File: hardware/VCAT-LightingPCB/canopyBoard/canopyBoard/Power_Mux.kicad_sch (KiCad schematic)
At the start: 6 parts, among them U15 TPS2117DRLR

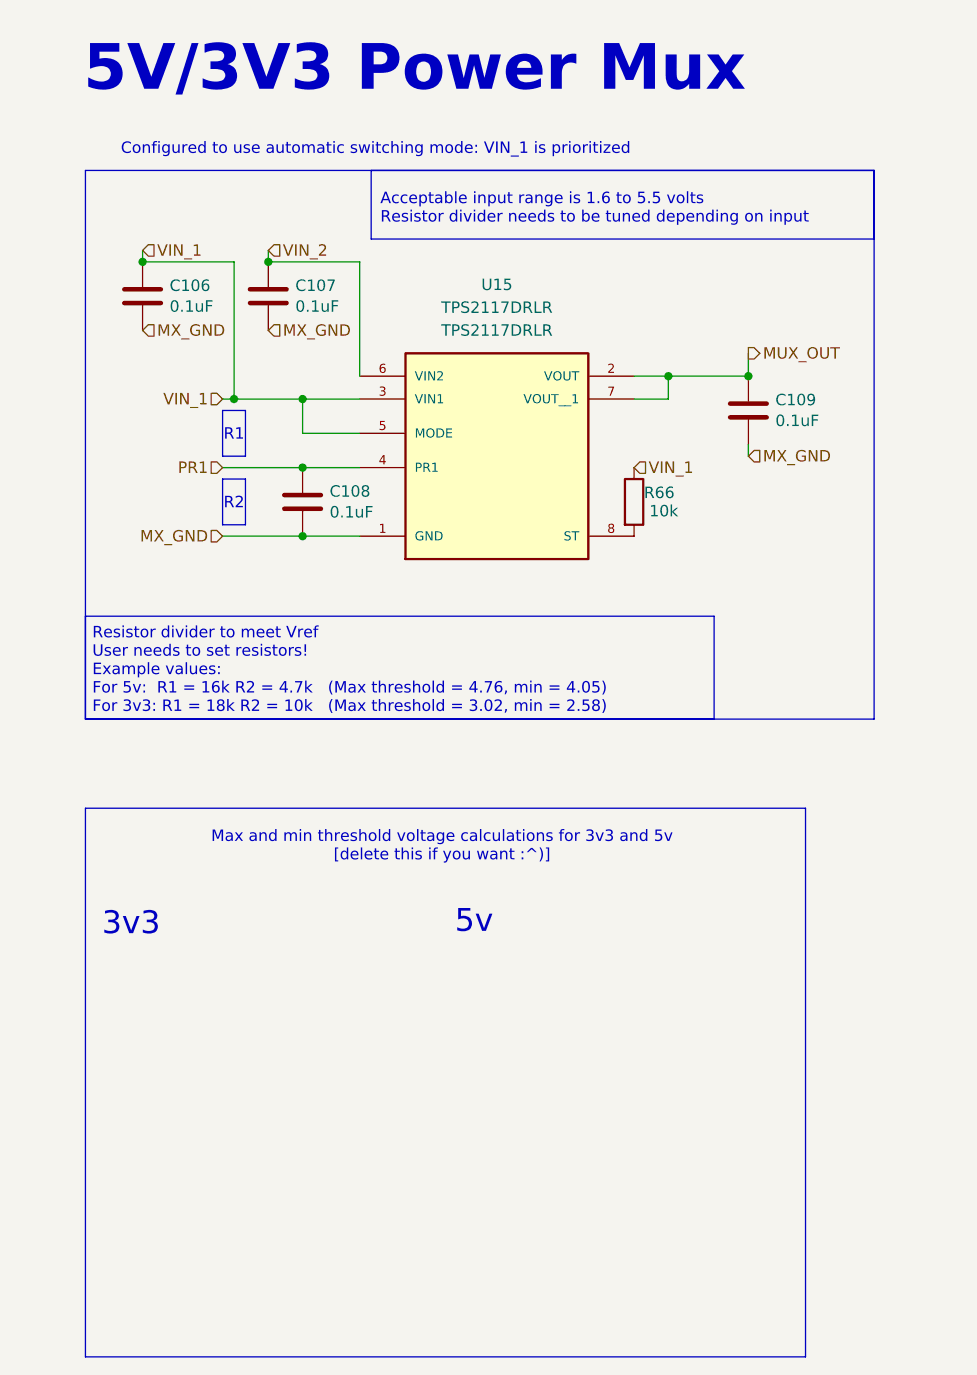
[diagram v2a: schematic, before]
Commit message: Untrack KiCad .history, convert KiCAD-Sharepoint to a submodule, remove LightsPCB
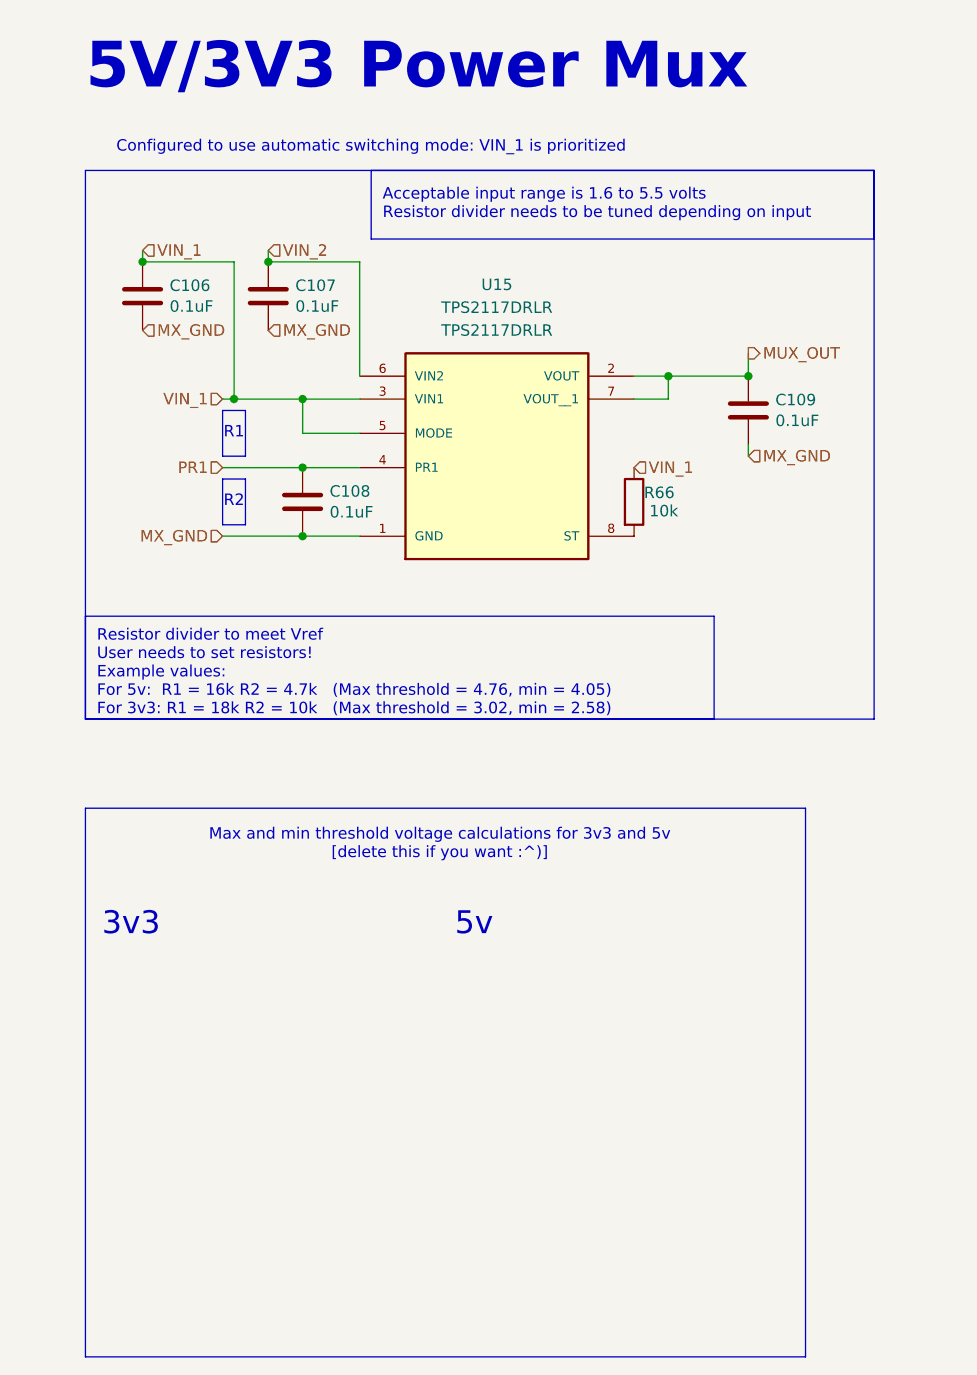
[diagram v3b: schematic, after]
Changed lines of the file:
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@@
 	(text "Max and min threshold voltage calculations for 3v3 and 5v\n[delete this if you want :^)]"
 		(exclude_from_sim no)
-		(at 54.864 106.934 0)
+		(at 54.61 106.68 0)
 		(effects
 			(font
@@
 	(text "R2"
 		(exclude_from_sim no)
-		(at 31.75 68.834 0)
+		(at 31.75 68.58 0)
 		(effects
 			(font
@@
 	(text "R1"
 		(exclude_from_sim no)
-		(at 31.75 61.214 0)
+		(at 31.75 60.96 0)
 		(effects
 			(font
@@
 	(text "5v "
 		(exclude_from_sim no)
-		(at 58.42 115.316 0)
+		(at 58.42 115.57 0)
 		(effects
 			(font
@@
 	(text "Configured to use automatic switching mode: VIN_1 is prioritized"
 		(exclude_from_sim no)
-		(at 47.498 29.464 0)
+		(at 46.99 29.21 0)
 		(effects
 			(font
@@
 	(text "Acceptable input range is 1.6 to 5.5 volts\nResistor divider needs to be tuned depending on input\n"
 		(exclude_from_sim no)
-		(at 48.006 36.068 0)
+		(at 48.26 35.56 0)
 		(effects
 			(font
@@
 	(text "Resistor divider to meet Vref \nUser needs to set resistors!\nExample values:\nFor 5v:  R1 = 16k R2 = 4.7k   (Max threshold = 4.76, min = 4.05)\nFor 3v3: R1 = 18k R2 = 10k   (Max threshold = 3.02, min = 2.58)"
 		(exclude_from_sim no)
-		(at 16.002 87.376 0)
+		(at 16.51 87.63 0)
 		(effects
 			(font
@@
 	(text "5V/3V3 Power Mux"
 		(exclude_from_sim no)
-		(at 51.816 20.574 0)
+		(at 52.07 20.32 0)
 		(effects
 			(font
